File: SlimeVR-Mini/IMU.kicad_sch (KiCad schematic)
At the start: 1 part, among them U2 BMI160

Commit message: IMU wiring done-ish
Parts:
- added C1: 100n, symbol Device:C
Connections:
- net SCL: now reaches U2.13 (SCX)
- net SDA: now reaches U2.14 (SDX)
- net SDX: now reaches U2.2 (ASDX)
- net SCX: now reaches U2.3 (ASCX)
- net +3V3: now reaches U2.5 (VDDIO)
- net +3V3: now also U2.8 (VDD), C1.2
- net GND: now reaches U2.6 (GNDIO)
- net GND: now also U2.7 (GND), C1.1
- no-connect marks 0 -> 6
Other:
- note added: "Does the IMU need an LDO reg? Or can we get away with good low noise board-wide 3V3?"
- note added: "Unused for now - can add magnetometer downstream for possibly better performance"
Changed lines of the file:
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@@
 (kicad_sch (version 20230121) (generator eeschema)
   (paper "A4")
+  (junction (at 161.29 86.36) (diameter 0) (color 0 0 0 0)
+  )
+  (junction (at 161.29 116.84) (diameter 0) (color 0 0 0 0)
+  )
+  (junction (at 161.29 83.82) (diameter 0) (color 0 0 0 0)
+  )
+  (no_connect (at 160.02 93.98))
+  (no_connect (at 160.02 96.52))
+  (no_connect (at 124.46 93.98))
+  (no_connect (at 124.46 109.22))
+  (no_connect (at 124.46 101.6))
+  (no_connect (at 124.46 106.68))
+  (wire (pts (xy 161.29 83.82) (xy 161.29 86.36))
+    (stroke (width 0) (type default))
+  )
+  (wire (pts (xy 160.02 114.3) (xy 161.29 114.3))
+    (stroke (width 0) (type default))
+  )
+  (wire (pts (xy 123.19 99.06) (xy 124.46 99.06))
+    (stroke (width 0) (type default))
+  )
+  (wire (pts (xy 161.29 116.84) (xy 161.29 118.11))
+    (stroke (width 0) (type default))
+  )
+  (wire (pts (xy 160.02 109.22) (xy 161.29 109.22))
+    (stroke (width 0) (type default))
+  )
+  (wire (pts (xy 160.02 116.84) (xy 161.29 116.84))
+    (stroke (width 0) (type default))
+  )
+  (wire (pts (xy 160.02 106.68) (xy 161.29 106.68))
+    (stroke (width 0) (type default))
+  )
+  (wire (pts (xy 168.91 83.82) (xy 170.18 83.82))
+    (stroke (width 0) (type default))
+  )
+  (wire (pts (xy 161.29 74.93) (xy 161.29 83.82))
+    (stroke (width 0) (type default))
+  )
+  (wire (pts (xy 161.29 114.3) (xy 161.29 116.84))
+    (stroke (width 0) (type default))
+  )
+  (wire (pts (xy 161.29 88.9) (xy 161.29 86.36))
+    (stroke (width 0) (type default))
+  )
+  (wire (pts (xy 160.02 88.9) (xy 161.29 88.9))
+    (stroke (width 0) (type default))
+  )
+  (wire (pts (xy 170.18 83.82) (xy 170.18 85.09))
+    (stroke (width 0) (type default))
+  )
+  (wire (pts (xy 161.29 86.36) (xy 160.02 86.36))
+    (stroke (width 0) (type default))
+  )
+  (wire (pts (xy 123.19 96.52) (xy 124.46 96.52))
+    (stroke (width 0) (type default))
+  )
+  (text "Unused for now - can add magnetometer\ndownstream for possibly better performance"
+    (at 166.37 109.22 0)
+    (effects (font (size 2 2)) (justify left bottom))
+  )
+  (text "Does the IMU need an LDO reg?\nOr can we get away with good\nlow noise board-wide 3V3?"
+    (at 165.1 78.74 0)
+    (effects (font (size 2 2)) (justify left bottom))
+  )
+  (label "SCX" (at 161.29 109.22 0) (fields_autoplaced)
+    (effects (font (size 1.27 1.27)) (justify left bottom))
+  )
+  (label "SDX" (at 161.29 106.68 0) (fields_autoplaced)
+    (effects (font (size 1.27 1.27)) (justify left bottom))
+  )
+  (hierarchical_label "SDA" (shape input) (at 123.19 99.06 180) (fields_autoplaced)
+    (effects (font (size 1.27 1.27)) (justify right))
+  )
+  (hierarchical_label "SCL" (shape input) (at 123.19 96.52 180) (fields_autoplaced)
+    (effects (font (size 1.27 1.27)) (justify right))
+  )
   (symbol (lib_id "Project Library:BMI160") (at 142.24 101.6 0) (unit 1)
     (in_bom yes) (on_board yes) (dnp no) (fields_autoplaced)
@@
         )
       )
+    )
+  )
+  (symbol (lib_id "power:GND") (at 161.29 118.11 0) (unit 1)
+    (in_bom yes) (on_board yes) (dnp no) (fields_autoplaced)
+    (property "Reference" "#PWR06" (at 161.29 124.46 0)
+      (effects (font (size 1.27 1.27)) hide)
+    )
+    (property "Value" "GND" (at 161.29 123.19 0)
+      (effects (font (size 1.27 1.27)))
+    )
+    (property "Footprint" "" (at 161.29 118.11 0)
+      (effects (font (size 1.27 1.27)) hide)
+    )
+    (property "Datasheet" "" (at 161.29 118.11 0)
+      (effects (font (size 1.27 1.27)) hide)
+    )
+    (pin "1")
+    (instances
+      (project "SlimeVR-Mini"
+        (path "/01f70e2f-47c6-495b-b6f7-eee456c9fb57"
+          (reference "#PWR06") (unit 1)
+        )
+        (path "/01f70e2f-47c6-495b-b6f7-eee456c9fb57/35e02d93-cdac-48f7-b47e-4a5ff7382a35"
+          (reference "#PWR06") (unit 1)
+        )
+        (path "/01f70e2f-47c6-495b-b6f7-eee456c9fb57/169517e7-20d5-4078-973c-5085edc66fe6"
+          (reference "#PWR09") (unit 1)
+        )
+      )
+    )
+  )
+  (symbol (lib_id "power:GND") (at 170.18 85.09 0) (unit 1)
+    (in_bom yes) (on_board yes) (dnp no) (fields_autoplaced)
+    (property "Reference" "#PWR06" (at 170.18 91.44 0)
+      (effects (font (size 1.27 1.27)) hide)
+    )
+    (property "Value" "GND" (at 170.18 90.17 0)
+      (effects (font (size 1.27 1.27)))
+    )
+    (property "Footprint" "" (at 170.18 85.09 0)
+      (effects (font (size 1.27 1.27)) hide)
+    )
+    (property "Datasheet" "" (at 170.18 85.09 0)
+      (effects (font (size 1.27 1.27)) hide)
+    )
+    (pin "1")
+    (instances
+      (project "SlimeVR-Mini"
+        (path "/01f70e2f-47c6-495b-b6f7-eee456c9fb57"
+          (reference "#PWR06") (unit 1)
+        )
+        (path "/01f70e2f-47c6-495b-b6f7-eee456c9fb57/35e02d93-cdac-48f7-b47e-4a5ff7382a35"
+          (reference "#PWR06") (unit 1)
+        )
+        (path "/01f70e2f-47c6-495b-b6f7-eee456c9fb57/169517e7-20d5-4078-973c-5085edc66fe6"
+          (reference "#PWR010") (unit 1)
+        )
+      )
+    )
+  )
+  (symbol (lib_id "power:+3V3") (at 161.29 74.93 0) (unit 1)
+    (in_bom yes) (on_board yes) (dnp no) (fields_autoplaced)
+    (property "Reference" "#PWR05" (at 161.29 78.74 0)
+      (effects (font (size 1.27 1.27)) hide)
+    )
+    (property "Value" "+3V3" (at 161.29 71.12 0)
+      (effects (font (size 1.27 1.27)))
+    )
+    (property "Footprint" "" (at 161.29 74.93 0)
+      (effects (font (size 1.27 1.27)) hide)
+    )
+    (property "Datasheet" "" (at 161.29 74.93 0)
+      (effects (font (size 1.27 1.27)) hide)
+    )
+    (pin "1")
+    (instances
+      (project "SlimeVR-Mini"
+        (path "/01f70e2f-47c6-495b-b6f7-eee456c9fb57"
+          (reference "#PWR05") (unit 1)
+        )
+        (path "/01f70e2f-47c6-495b-b6f7-eee456c9fb57/35e02d93-cdac-48f7-b47e-4a5ff7382a35"
+          (reference "#PWR05") (unit 1)
+        )
+        (path "/01f70e2f-47c6-495b-b6f7-eee456c9fb57/169517e7-20d5-4078-973c-5085edc66fe6"
+          (reference "#PWR08") (unit 1)
+        )
+      )
+    )
+  )
+  (symbol (lib_id "Device:C") (at 165.1 83.82 270) (unit 1)
+    (in_bom yes) (on_board yes) (dnp no)
+    (property "Reference" "C1" (at 162.56 82.55 90)
+      (effects (font (size 1.27 1.27)))
+    )
+    (property "Value" "100n" (at 168.91 82.55 90)
+      (effects (font (size 1.27 1.27)))
+    )
+    (property "Footprint" "" (at 161.29 84.7852 0)
+      (effects (font (size 1.27 1.27)) hide)
+    )
+    (property "Datasheet" "~" (at 165.1 83.82 0)
+      (effects (font (size 1.27 1.27)) hide)
+    )
+    (pin "1")
+    (pin "2")
+    (instances
+      (project "SlimeVR-Mini"
+        (path "/01f70e2f-47c6-495b-b6f7-eee456c9fb57"
+          (reference "C1") (unit 1)
+        )
+        (path "/01f70e2f-47c6-495b-b6f7-eee456c9fb57/35e02d93-cdac-48f7-b47e-4a5ff7382a35"
+          (reference "C1") (unit 1)
+        )
+        (path "/01f70e2f-47c6-495b-b6f7-eee456c9fb57/169517e7-20d5-4078-973c-5085edc66fe6"
+          (reference "C4") (unit 1)
+        )
+      )

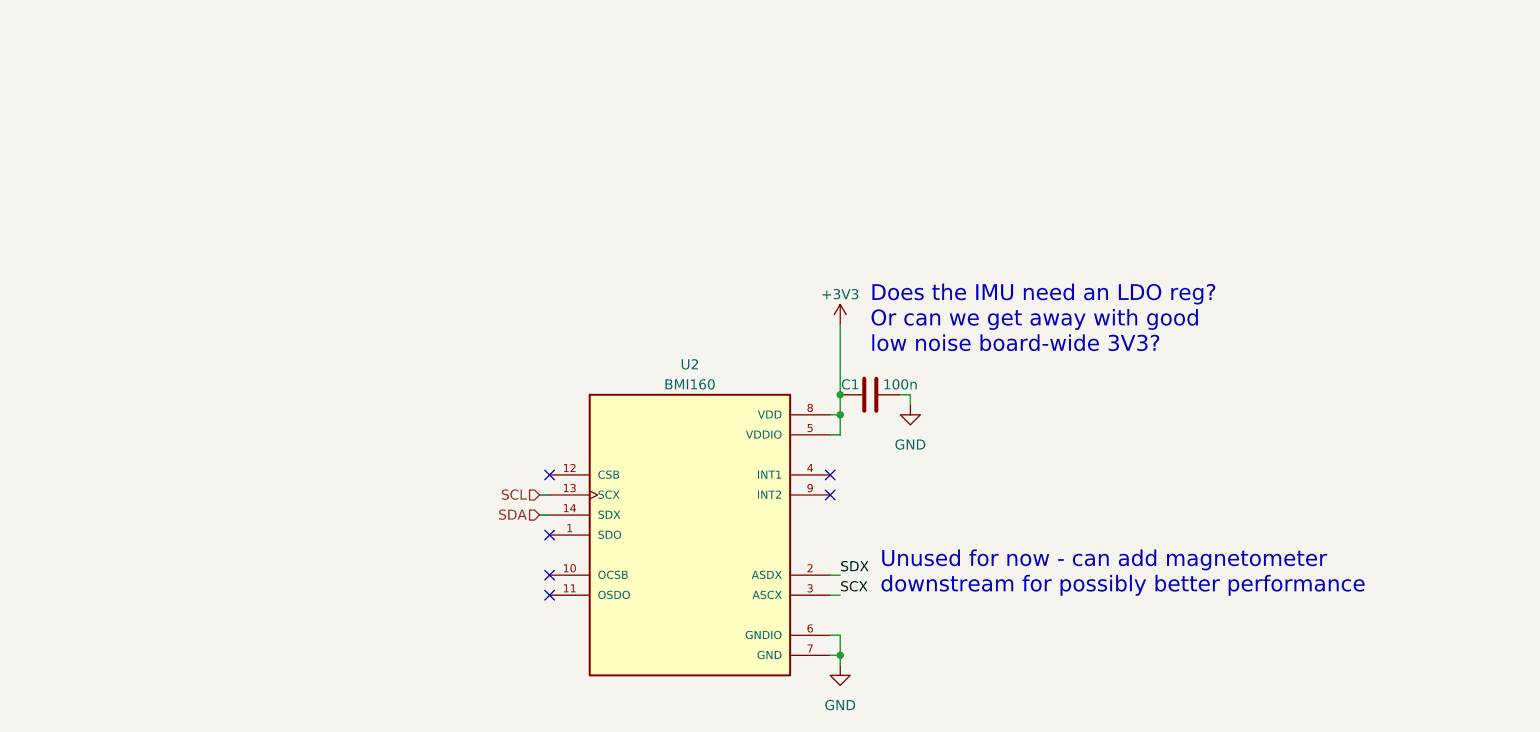
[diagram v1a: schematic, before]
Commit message: added Power page + fixing symbols and footprints
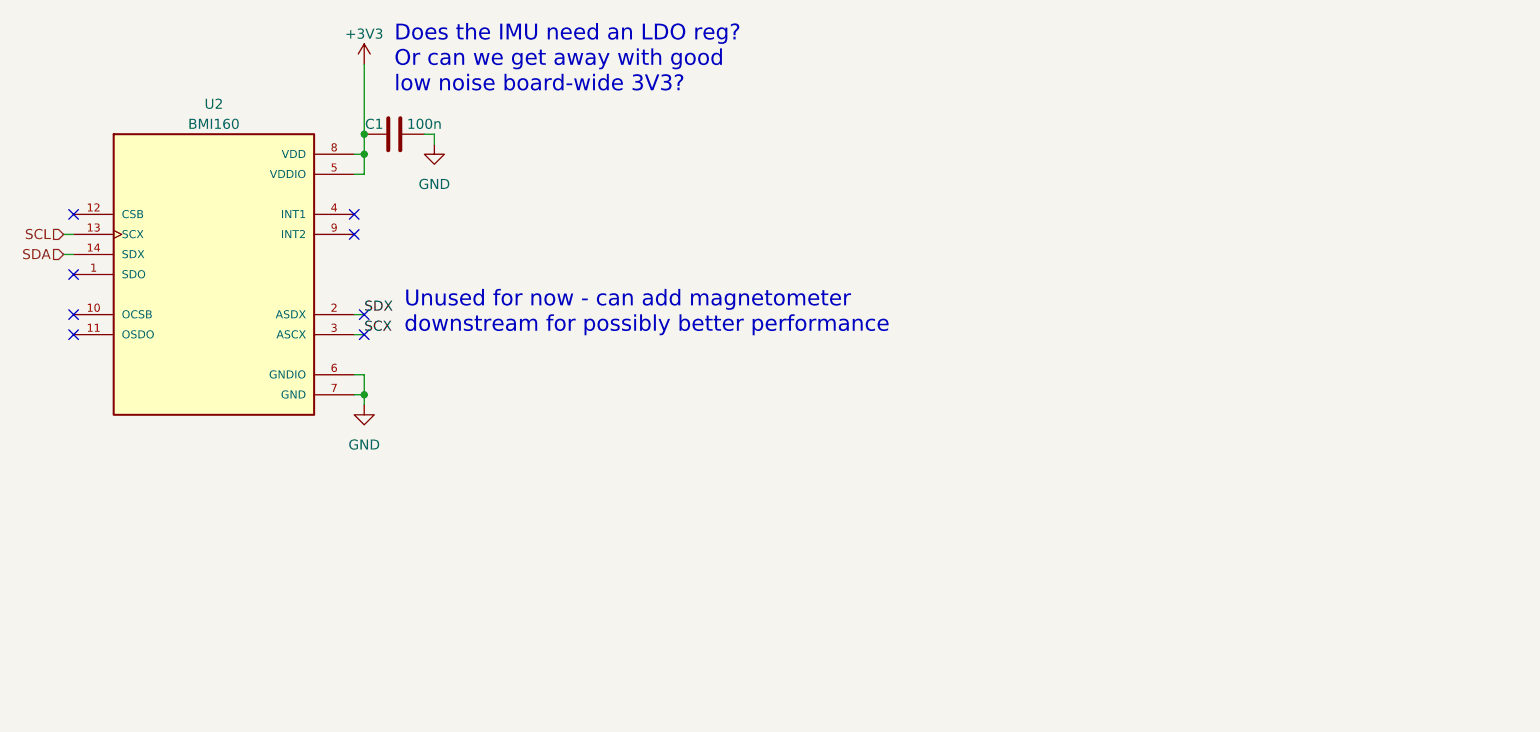
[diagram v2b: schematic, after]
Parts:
- U2: footprint BMI160:PQFN50P250X300X88-14N -> Project Library:PQFN50P250X300X88-14N
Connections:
- no-connect marks 6 -> 8
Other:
- moved on the sheet: C1, U2

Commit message: assigned footprints, finished USB-UART sch
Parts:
- C1: footprint (none) -> Capacitor_SMD:C_0402_1005Metric
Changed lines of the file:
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@@
       (effects (font (size 1.27 1.27)))
     )
-    (property "Footprint" "" (at 100.965 51.7652 0)
+    (property "Footprint" "Capacitor_SMD:C_0402_1005Metric" (at 100.965 51.7652 0)
       (effects (font (size 1.27 1.27)) hide)
     )
